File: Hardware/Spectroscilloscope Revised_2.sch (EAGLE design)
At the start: 48 parts, among them IC1 7805TV, Q1 16MHz, U1 ATMEGA328P-PU, U2 MCP6024-I/P, U3 MCP6024-I/P

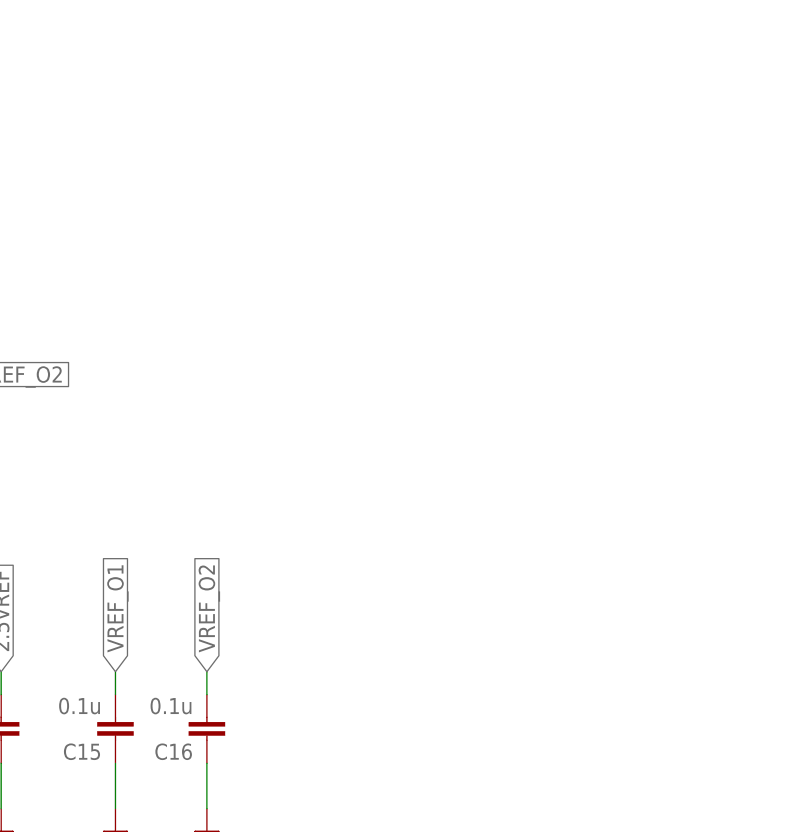
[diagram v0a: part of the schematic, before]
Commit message: Schematics Update - Code Clean up - MCP3004 data Acquisition
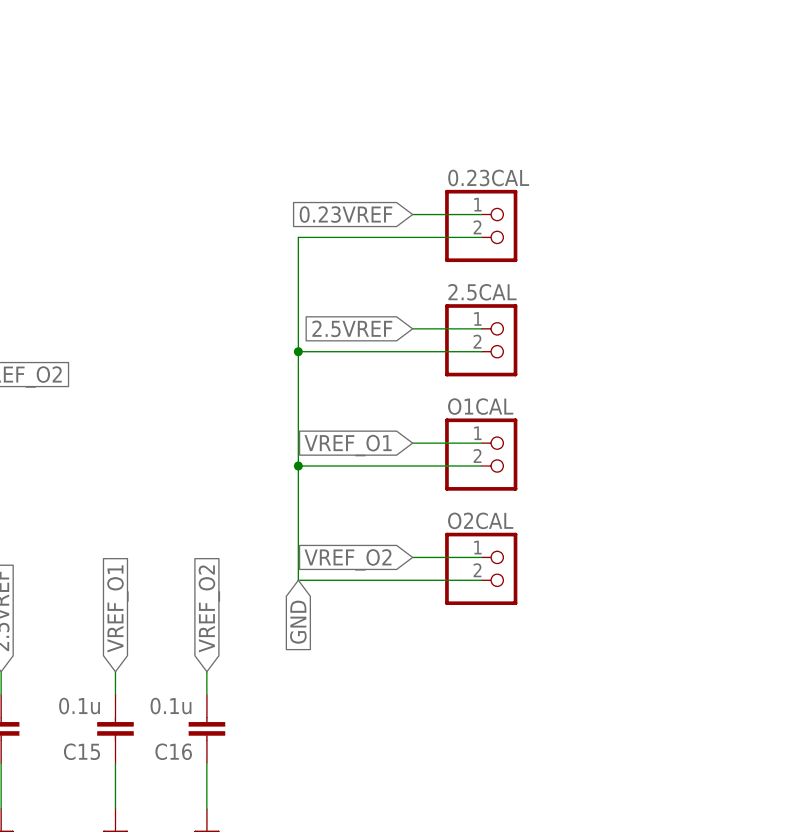
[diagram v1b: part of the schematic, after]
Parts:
- added 0.23CAL, 2.5CAL, O1CAL, O2CAL: (no value), pinhead:PINHD-1X2
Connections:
- net 0.23VREF: now also 0.23CAL.1
- net 2.5VREF: now also 2.5CAL.1
- net GND: now also 0.23CAL.2, 2.5CAL.2, O1CAL.2, O2CAL.2
- net VREF_O1: now also O1CAL.1
- net VREF_O2: now also O2CAL.1
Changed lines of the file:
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@@
 <part name="SUPPLY26" library="supply2" library_urn="urn:adsk.eagle:library:372" deviceset="GND" device=""/>
 <part name="INPUT" library="5-1634503-1" deviceset="5-1634503-1" device=""/>
+<part name="0.23CAL" library="pinhead" library_urn="urn:adsk.eagle:library:325" deviceset="PINHD-1X2" device="" package3d_urn="urn:adsk.eagle:package:22435/2"/>
+<part name="2.5CAL" library="pinhead" library_urn="urn:adsk.eagle:library:325" deviceset="PINHD-1X2" device="" package3d_urn="urn:adsk.eagle:package:22435/2"/>
+<part name="O1CAL" library="pinhead" library_urn="urn:adsk.eagle:library:325" deviceset="PINHD-1X2" device="" package3d_urn="urn:adsk.eagle:package:22435/2"/>
+<part name="O2CAL" library="pinhead" library_urn="urn:adsk.eagle:library:325" deviceset="PINHD-1X2" device="" package3d_urn="urn:adsk.eagle:package:22435/2"/>
 </parts>
 <sheets>
@@
 <attribute name="NAME" x="-314.459309375" y="-19.80306875" size="1.780840625" layer="95"/>
 <attribute name="VALUE" x="-314.71346875" y="-33.031790625" size="1.78075" layer="96"/>
+</instance>
+<instance part="0.23CAL" gate="G$1" x="-124.46" y="-218.44" smashed="yes">
+<attribute name="NAME" x="-130.81" y="-212.725" size="1.778" layer="95"/>
+<attribute name="VALUE" x="-130.81" y="-223.52" size="1.778" layer="96"/>
+</instance>
+<instance part="2.5CAL" gate="G$1" x="-124.46" y="-231.14" smashed="yes">
+<attribute name="NAME" x="-130.81" y="-225.425" size="1.778" layer="95"/>
+<attribute name="VALUE" x="-130.81" y="-236.22" size="1.778" layer="96"/>
+</instance>
+<instance part="O1CAL" gate="G$1" x="-124.46" y="-243.84" smashed="yes">
+<attribute name="NAME" x="-130.81" y="-238.125" size="1.778" layer="95"/>
+<attribute name="VALUE" x="-130.81" y="-248.92" size="1.778" layer="96"/>
+</instance>
+<instance part="O2CAL" gate="G$1" x="-124.46" y="-256.54" smashed="yes">
+<attribute name="NAME" x="-130.81" y="-250.825" size="1.778" layer="95"/>
+<attribute name="VALUE" x="-130.81" y="-261.62" size="1.778" layer="96"/>
 </instance>
 </instances>
@@
 <pinref part="C16" gate="G$1" pin="1"/>
 <wire x1="-157.48" y1="-281.94" x2="-157.48" y2="-276.86" width="0.1524" layer="91"/>
+</segment>
+<segment>
+<pinref part="0.23CAL" gate="G$1" pin="2"/>
+<wire x1="-127" y1="-218.44" x2="-147.32" y2="-218.44" width="0.1524" layer="91"/>
+<wire x1="-147.32" y1="-218.44" x2="-147.32" y2="-231.14" width="0.1524" layer="91"/>
+<pinref part="2.5CAL" gate="G$1" pin="2"/>
+<wire x1="-147.32" y1="-231.14" x2="-127" y2="-231.14" width="0.1524" layer="91"/>
+<pinref part="O1CAL" gate="G$1" pin="2"/>
+<wire x1="-147.32" y1="-231.14" x2="-147.32" y2="-243.84" width="0.1524" layer="91"/>
+<wire x1="-147.32" y1="-243.84" x2="-127" y2="-243.84" width="0.1524" layer="91"/>
+<junction x="-147.32" y="-231.14"/>
+<pinref part="O2CAL" gate="G$1" pin="2"/>
+<wire x1="-147.32" y1="-243.84" x2="-147.32" y2="-256.54" width="0.1524" layer="91"/>
+<wire x1="-147.32" y1="-256.54" x2="-127" y2="-256.54" width="0.1524" layer="91"/>
+<junction x="-147.32" y="-243.84"/>
+<label x="-147.32" y="-256.54" size="1.778" layer="95" rot="R270" xref="yes"/>
 </segment>
 </net>
@@
 <label x="-193.04" y="-266.7" size="1.778" layer="95" rot="R90" xref="yes"/>
 </segment>
+<segment>
+<pinref part="0.23CAL" gate="G$1" pin="1"/>
+<wire x1="-127" y1="-215.9" x2="-134.62" y2="-215.9" width="0.1524" layer="91"/>
+<label x="-134.62" y="-215.9" size="1.778" layer="95" rot="R180" xref="yes"/>
+</segment>
 </net>
 <net name="2.5VREF" class="0">
@@
 <label x="-271.78" y="-68.58" size="1.778" layer="95" rot="R180" xref="yes"/>
 </segment>
+<segment>
+<pinref part="2.5CAL" gate="G$1" pin="1"/>
+<wire x1="-127" y1="-228.6" x2="-134.62" y2="-228.6" width="0.1524" layer="91"/>
+<label x="-134.62" y="-228.6" size="1.778" layer="95" rot="R180" xref="yes"/>
+</segment>
 </net>
 <net name="VREF_O1" class="0">
@@
 <label x="-167.64" y="-266.7" size="1.778" layer="95" rot="R90" xref="yes"/>
 </segment>
+<segment>
+<pinref part="O1CAL" gate="G$1" pin="1"/>
+<wire x1="-127" y1="-241.3" x2="-134.62" y2="-241.3" width="0.1524" layer="91"/>
+<label x="-134.62" y="-241.3" size="1.778" layer="95" rot="R180" xref="yes"/>
+</segment>
 </net>
 <net name="VREF_O2" class="0">
@@
 <label x="-157.48" y="-266.7" size="1.778" layer="95" rot="R90" xref="yes"/>
 </segment>
-</net>
+<segment>
+<pinref part="O2CAL" gate="G$1" pin="1"/>
+<wire x1="-127" y1="-254" x2="-134.62" y2="-254" width="0.1524" layer="91"/>
+<label x="-134.62" y="-254" size="1.778" layer="95" rot="R180" xref="yes"/>
+</segment>
+</net>

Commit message: Wroked on PCB, updated Schematic
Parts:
- added CAPTURING, POWER: (no value), led:LED5MM
- added R12, R13: 330, rcl:R-EU_0204/7
- C10, C8, C9: device capacitor-wima:C2,5-3 -> rcl:C-EU050-024X044
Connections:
- removed net N$11: R8.2, U1.PD1
- new net N$12: POWER.C, R12.2
- new net N$13: CAPTURING.C, R13.2
- new net N$14: CAPTURING.A, U1.PD4
- net GND: now also R12.1, R13.1
- net VCC: now also POWER.A
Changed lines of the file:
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@@
 </variantdefs>
 <classes>
-<class number="0" name="default" width="0" drill="0">
+<class number="0" name="default" width="0.4064" drill="0">
+<clearance class="0" value="0.1016"/>
 </class>
-<class number="1" name="Power Lines" width="0.3048" drill="0">
-<clearance class="1" value="0.0508"/>
+<class number="1" name="Power Lines" width="0.762" drill="0">
+<clearance class="1" value="0.129540625"/>
 </class>
 </classes>
@@
 <part name="SUPPLY13" library="supply2" library_urn="urn:adsk.eagle:library:372" deviceset="GND" device=""/>
 <part name="SUPPLY14" library="supply2" library_urn="urn:adsk.eagle:library:372" deviceset="GND" device=""/>
-<part name="C8" library="capacitor-wima" library_urn="urn:adsk.eagle:library:116" deviceset="C" device="2,5-3" package3d_urn="urn:adsk.eagle:package:5436/1" value="0.1uF"/>
-<part name="C9" library="capacitor-wima" library_urn="urn:adsk.eagle:library:116" deviceset="C" device="2,5-3" package3d_urn="urn:adsk.eagle:package:5436/1" value="10uF"/>
-<part name="C10" library="capacitor-wima" library_urn="urn:adsk.eagle:library:116" deviceset="C" device="2,5-3" package3d_urn="urn:adsk.eagle:package:5436/1" value="220uF"/>
+<part name="C8" library="rcl" library_urn="urn:adsk.eagle:library:334" deviceset="C-EU" device="050-024X044" package3d_urn="urn:adsk.eagle:package:23643/1" value="0.1uF"/>
+<part name="C9" library="rcl" library_urn="urn:adsk.eagle:library:334" deviceset="C-EU" device="050-024X044" package3d_urn="urn:adsk.eagle:package:23643/1" value="10uF"/>
+<part name="C10" library="rcl" library_urn="urn:adsk.eagle:library:334" deviceset="C-EU" device="050-024X044" package3d_urn="urn:adsk.eagle:package:23643/1" value="220uF"/>
 <part name="P+13" library="supply1" deviceset="+12V" device=""/>
 <part name="P+14" library="supply1" library_urn="urn:adsk.eagle:library:371" deviceset="VCC" device=""/>
@@
 <part name="O1CAL" library="pinhead" library_urn="urn:adsk.eagle:library:325" deviceset="PINHD-1X2" device="" package3d_urn="urn:adsk.eagle:package:22435/2"/>
 <part name="O2CAL" library="pinhead" library_urn="urn:adsk.eagle:library:325" deviceset="PINHD-1X2" device="" package3d_urn="urn:adsk.eagle:package:22435/2"/>
+<part name="POWER" library="led" library_urn="urn:adsk.eagle:library:259" deviceset="LED" device="5MM" package3d_urn="urn:adsk.eagle:package:15799/2"/>
+<part name="R12" library="rcl" library_urn="urn:adsk.eagle:library:334" deviceset="R-EU_" device="0204/7" package3d_urn="urn:adsk.eagle:package:23498/2" value="330"/>
+<part name="R13" library="rcl" library_urn="urn:adsk.eagle:library:334" deviceset="R-EU_" device="0204/7" package3d_urn="urn:adsk.eagle:package:23498/2" value="330"/>
+<part name="CAPTURING" library="led" library_urn="urn:adsk.eagle:library:259" deviceset="LED" device="5MM" package3d_urn="urn:adsk.eagle:package:15799/2"/>
 </parts>
 <sheets>
@@
 <attribute name="VALUE" x="-130.81" y="-261.62" size="1.778" layer="96"/>
 </instance>
+<instance part="POWER" gate="G$1" x="-88.9" y="53.34" smashed="yes">
+<attribute name="NAME" x="-85.344" y="48.768" size="1.778" layer="95" rot="R90"/>
+<attribute name="VALUE" x="-83.185" y="48.768" size="1.778" layer="96" rot="R90"/>
+</instance>
+<instance part="R12" gate="G$1" x="-88.9" y="38.1" smashed="yes" rot="R90">
+<attribute name="NAME" x="-90.3986" y="34.29" size="1.778" layer="95" rot="R90"/>
+<attribute name="VALUE" x="-85.598" y="34.29" size="1.778" layer="96" rot="R90"/>
+</instance>
+<instance part="R13" gate="G$1" x="33.02" y="-7.62" smashed="yes" rot="R180">
+<attribute name="NAME" x="36.83" y="-9.1186" size="1.778" layer="95" rot="R180"/>
+<attribute name="VALUE" x="36.83" y="-4.318" size="1.778" layer="96" rot="R180"/>
+</instance>
+<instance part="CAPTURING" gate="G$1" x="25.4" y="0" smashed="yes">
+<attribute name="NAME" x="28.956" y="-4.572" size="1.778" layer="95" rot="R90"/>
+<attribute name="VALUE" x="31.115" y="-4.572" size="1.778" layer="96" rot="R90"/>
+</instance>
 </instances>
 <busses>
@@
 </segment>
 </net>
-<net name="GND" class="0">
+<net name="GND" class="1">
 <segment>
 <pinref part="C1" gate="G$1" pin="1"/>
@@
 <pinref part="R9" gate="G$1" pin="2"/>
 <wire x1="48.26" y1="-2.54" x2="48.26" y2="0" width="0.1524" layer="91"/>
+<wire x1="45.72" y1="-7.62" x2="45.72" y2="-2.54" width="0.1524" layer="91"/>
+<wire x1="45.72" y1="-2.54" x2="48.26" y2="-2.54" width="0.1524" layer="91"/>
+<junction x="48.26" y="-2.54"/>
+<pinref part="R13" gate="G$1" pin="1"/>
+<wire x1="38.1" y1="-7.62" x2="45.72" y2="-7.62" width="0.1524" layer="91"/>
 </segment>
 <segment>
@@
 <wire x1="-104.14" y1="45.72" x2="-114.3" y2="45.72" width="0.1524" layer="91"/>
 <junction x="-114.3" y="45.72"/>
+<pinref part="R12" gate="G$1" pin="1"/>
+<wire x1="-88.9" y1="33.02" x2="-104.14" y2="33.02" width="0.1524" layer="91"/>
+<wire x1="-104.14" y1="33.02" x2="-104.14" y2="45.72" width="0.1524" layer="91"/>
+<junction x="-104.14" y="45.72"/>
 </segment>
 <segment>
@@
 </segment>
 </net>
-<net name="VCC" class="0">
+<net name="VCC" class="1">
 <segment>
 <pinref part="P+1" gate="VCC" pin="VCC"/>
@@
 <wire x1="-104.14" y1="67.056" x2="-104.14" y2="60.96" width="0.1524" layer="91"/>
 <junction x="-104.14" y="60.96"/>
+<pinref part="POWER" gate="G$1" pin="A"/>
+<wire x1="-88.9" y1="55.88" x2="-88.9" y2="60.96" width="0.1524" layer="91"/>
+<wire x1="-88.9" y1="60.96" x2="-104.14" y2="60.96" width="0.1524" layer="91"/>
 </segment>
 <segment>
@@
 <segment>
 <pinref part="U1" gate="A" pin="PD0"/>
-<wire x1="17.78" y1="15.24" x2="40.64" y2="15.24" width="0.1524" layer="91"/>
-<label x="40.64" y="15.24" size="1.778" layer="95" xref="yes"/>
+<wire x1="17.78" y1="15.24" x2="40.64" y2="10.16" width="0.1524" layer="91"/>
+<label x="40.64" y="10.16" size="1.778" layer="95" xref="yes"/>
 </segment>
 </net>
@@
 <wire x1="104.14" y1="-2.54" x2="96.52" y2="-2.54" width="0.1524" layer="91"/>
 <label x="96.52" y="-2.54" size="1.778" layer="95" rot="R180"/>
-</segment>
-</net>
-<net name="N$11" class="0">
-<segment>
-<pinref part="R8" gate="G$1" pin="2"/>
-<pinref part="U1" gate="A" pin="PD1"/>
-<wire x1="27.94" y1="12.7" x2="17.78" y2="12.7" width="0.1524" layer="91"/>
 </segment>
 </net>
@@
 </segment>
 </net>
-<net name="+12V" class="0">
+<net name="+12V" class="1">
 <segment>
 <pinref part="C10" gate="G$1" pin="1"/>
@@
 </segment>
 </net>
-<net name="+12VI" class="0">
+<net name="+12VI" class="1">
 <segment>
 <wire x1="-180.34" y1="66.04" x2="-180.34" y2="63.5" width="0.1524" layer="91"/>
@@
 </segment>
 </net>
+<net name="N$12" class="0">
+<segment>
+<pinref part="R12" gate="G$1" pin="2"/>
+<pinref part="POWER" gate="G$1" pin="C"/>
+<wire x1="-88.9" y1="43.18" x2="-88.9" y2="48.26" width="0.1524" layer="91"/>
+</segment>
+</net>
+<net name="N$13" class="0">
+<segment>
+<pinref part="R13" gate="G$1" pin="2"/>
+<wire x1="27.94" y1="-7.62" x2="25.4" y2="-7.62" width="0.1524" layer="91"/>
+<pinref part="CAPTURING" gate="G$1" pin="C"/>
+<wire x1="25.4" y1="-7.62" x2="25.4" y2="-5.08" width="0.1524" layer="91"/>
+</segment>
+</net>
+<net name="N$14" class="0">
+<segment>
+<pinref part="U1" gate="A" pin="PD4"/>
+<wire x1="17.78" y1="5.08" x2="25.4" y2="5.08" width="0.1524" layer="91"/>
+<pinref part="CAPTURING" gate="G$1" pin="A"/>
+<wire x1="25.4" y1="5.08" x2="25.4" y2="2.54" width="0.1524" layer="91"/>
+</segment>
+</net>

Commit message: Updated Schematics
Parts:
- added PROBECON: (no value), pinhead:PINHD-2X3
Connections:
- net +12VI: now also 12VPOWER.1; no longer 12VPOWER.2, 12VPOWER.3
- net GND: now also 12VPOWER.2, 12VPOWER.3, PROBECON.1, PROBECON.2, PROBECON.3, PROBECON.4, PROBECON.5; no longer 12VPOWER.1
- net VIN: now also PROBECON.6
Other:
- moved on the sheet: 12VPOWER
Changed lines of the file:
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@@
 <part name="R13" library="rcl" library_urn="urn:adsk.eagle:library:334" deviceset="R-EU_" device="0204/7" package3d_urn="urn:adsk.eagle:package:23498/2" value="330"/>
 <part name="CAPTURING" library="led" library_urn="urn:adsk.eagle:library:259" deviceset="LED" device="5MM" package3d_urn="urn:adsk.eagle:package:15799/2"/>
+<part name="PROBECON" library="pinhead" library_urn="urn:adsk.eagle:library:325" deviceset="PINHD-2X3" device="" package3d_urn="urn:adsk.eagle:package:22462/2"/>
 </parts>
 <sheets>
@@
 <attribute name="VALUE" x="-40.64" y="-63.5" size="1.778" layer="96" rot="R90"/>
 </instance>
-<instance part="12VPOWER" gate="G$1" x="-172.72" y="58.42" smashed="yes" rot="R180">
-<attribute name="NAME" x="-170.18" y="54.61" size="1.778" layer="95"/>
-<attribute name="VALUE" x="-213.36" y="62.23" size="1.778" layer="96" rot="R180"/>
+<instance part="12VPOWER" gate="G$1" x="-187.96" y="58.42" smashed="yes">
+<attribute name="NAME" x="-190.5" y="62.23" size="1.778" layer="95" rot="R180"/>
+<attribute name="VALUE" x="-147.32" y="54.61" size="1.778" layer="96"/>
 </instance>
 <instance part="P+11" gate="1" x="-180.34" y="68.58" smashed="yes"/>
@@
 <attribute name="NAME" x="28.956" y="-4.572" size="1.778" layer="95" rot="R90"/>
 <attribute name="VALUE" x="31.115" y="-4.572" size="1.778" layer="96" rot="R90"/>
+</instance>
+<instance part="PROBECON" gate="A" x="-309.88" y="-48.26" smashed="yes">
+<attribute name="NAME" x="-316.23" y="-42.545" size="1.778" layer="95"/>
+<attribute name="VALUE" x="-316.23" y="-55.88" size="1.778" layer="96"/>
 </instance>
 </instances>
@@
 <wire x1="55.88" y1="-129.54" x2="55.88" y2="-134.62" width="0.1524" layer="91"/>
 <pinref part="SUPPLY20" gate="GND" pin="GND"/>
-</segment>
-<segment>
-<pinref part="SUPPLY13" gate="GND" pin="GND"/>
-<pinref part="12VPOWER" gate="G$1" pin="1"/>
-<wire x1="-180.34" y1="53.34" x2="-180.34" y2="55.88" width="0.1524" layer="91"/>
 </segment>
 <segment>
@@
 <junction x="-147.32" y="-243.84"/>
 <label x="-147.32" y="-256.54" size="1.778" layer="95" rot="R270" xref="yes"/>
+</segment>
+<segment>
+<pinref part="12VPOWER" gate="G$1" pin="2"/>
+<pinref part="12VPOWER" gate="G$1" pin="3"/>
+<wire x1="-180.34" y1="58.42" x2="-180.34" y2="55.88" width="0.1524" layer="91"/>
+<pinref part="SUPPLY13" gate="GND" pin="GND"/>
+<wire x1="-180.34" y1="53.34" x2="-180.34" y2="55.88" width="0.1524" layer="91"/>
+<junction x="-180.34" y="55.88"/>
+</segment>
+<segment>
+<pinref part="PROBECON" gate="A" pin="1"/>
+<wire x1="-312.42" y1="-45.72" x2="-322.58" y2="-45.72" width="0.1524" layer="91"/>
+<pinref part="PROBECON" gate="A" pin="3"/>
+<wire x1="-322.58" y1="-45.72" x2="-322.58" y2="-48.26" width="0.1524" layer="91"/>
+<wire x1="-322.58" y1="-48.26" x2="-312.42" y2="-48.26" width="0.1524" layer="91"/>
+<pinref part="PROBECON" gate="A" pin="5"/>
+<wire x1="-322.58" y1="-48.26" x2="-322.58" y2="-50.8" width="0.1524" layer="91"/>
+<wire x1="-322.58" y1="-50.8" x2="-312.42" y2="-50.8" width="0.1524" layer="91"/>
+<junction x="-322.58" y="-48.26"/>
+<pinref part="PROBECON" gate="A" pin="2"/>
+<wire x1="-304.8" y1="-45.72" x2="-297.18" y2="-45.72" width="0.1524" layer="91"/>
+<wire x1="-297.18" y1="-45.72" x2="-297.18" y2="-38.1" width="0.1524" layer="91"/>
+<wire x1="-297.18" y1="-38.1" x2="-322.58" y2="-38.1" width="0.1524" layer="91"/>
+<wire x1="-322.58" y1="-38.1" x2="-322.58" y2="-45.72" width="0.1524" layer="91"/>
+<junction x="-322.58" y="-45.72"/>
+<pinref part="PROBECON" gate="A" pin="4"/>
+<wire x1="-304.8" y1="-48.26" x2="-297.18" y2="-48.26" width="0.1524" layer="91"/>
+<wire x1="-297.18" y1="-48.26" x2="-297.18" y2="-45.72" width="0.1524" layer="91"/>
+<junction x="-297.18" y="-45.72"/>
+<label x="-297.18" y="-38.1" size="1.778" layer="95" xref="yes"/>
 </segment>
 </net>
@@
 <wire x1="-271.78" y1="-22.86" x2="-254" y2="-22.86" width="0.1524" layer="91"/>
 </segment>
+<segment>
+<pinref part="PROBECON" gate="A" pin="6"/>
+<wire x1="-304.8" y1="-50.8" x2="-297.18" y2="-50.8" width="0.1524" layer="91"/>
+<label x="-297.18" y="-50.8" size="1.778" layer="95" xref="yes"/>
+</segment>
 </net>
 <net name="1X/10X" class="0">
@@
 <segment>
 <wire x1="-180.34" y1="66.04" x2="-180.34" y2="63.5" width="0.1524" layer="91"/>
-<wire x1="-180.34" y1="63.5" x2="-180.34" y2="60.96" width="0.1524" layer="91"/>
-<wire x1="-180.34" y1="60.96" x2="-180.34" y2="58.42" width="0.1524" layer="91"/>
-<junction x="-180.34" y="60.96"/>
 <pinref part="P+11" gate="1" pin="+12V"/>
-<pinref part="12VPOWER" gate="G$1" pin="2"/>
-<pinref part="12VPOWER" gate="G$1" pin="3"/>
 <wire x1="-180.34" y1="63.5" x2="-165.1" y2="63.5" width="0.1524" layer="91"/>
-<junction x="-180.34" y="63.5"/>
 <pinref part="SPST" gate="-1" pin="K"/>
 <wire x1="-165.1" y1="63.5" x2="-165.1" y2="68.58" width="0.1524" layer="91"/>
 <label x="-180.34" y="66.04" size="1.778" layer="95" rot="R180"/>
-</segment>
-</net>
+<pinref part="12VPOWER" gate="G$1" pin="1"/>
+<wire x1="-180.34" y1="60.96" x2="-180.34" y2="63.5" width="0.1524" layer="91"/>
+<junction x="-180.34" y="63.5"/>
+</segment>
+</net>

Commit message: Revised the Front end design - Final revision - multisim simulation works - Testing Breadboard April 21
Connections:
- new net N$11: R3.1, R4.2
- new net N$17: R8.2, U1.PC1
- net NONINV: no longer R3.1, R4.2
- net TX: now also U1.PC0; no longer U1.PD0
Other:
- moved on the sheet: C4, C5, C7, D1, D2, INPUT, PROBECON, R3, R4
